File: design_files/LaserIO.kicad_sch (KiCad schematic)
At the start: 25 parts, among them J10 DA15_Receptacle, J11 DB25_Receptacle, U4 74HC245, U5 UA9638CD, U6 UA9638CD, U7 74LVC1G3208

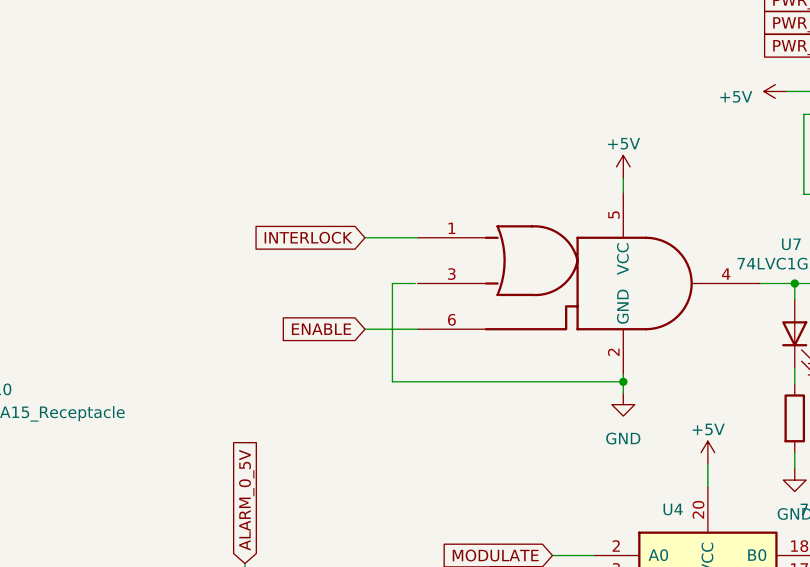
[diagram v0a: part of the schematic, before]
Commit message: And that's why we write documentation - two small errors on the pcb
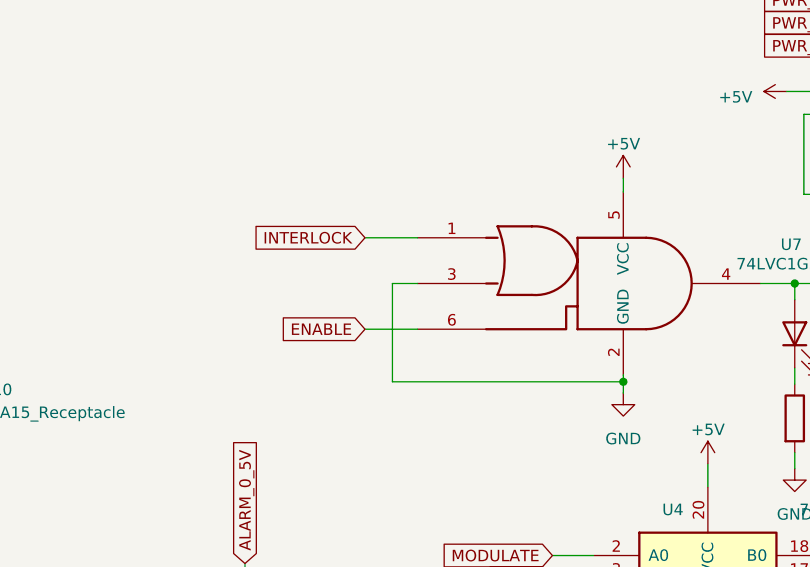
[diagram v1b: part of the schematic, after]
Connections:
- net GND: now also U7.3
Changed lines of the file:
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@@
-    (stroke (width 0) (type default))
-  )
-  (wire (pts (xy 150.368 72.898) (xy 147.828 72.898))
     (stroke (width 0) (type default))
   )
@@
     (stroke (width 0) (type default))
   )
+  (wire (pts (xy 147.828 72.898) (xy 150.622 72.898))
+    (stroke (width 0) (type default))
+  )

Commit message: BOM, readme update
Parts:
- C10, C7, C8, C9: value 0.1uF, 16V -> 0.1uF, 25V; MouserPN (none) -> 187-CL05A104KA5NNNC; mpn (none) -> CL05A104KA5NNNC
- D17: mpn (none) -> 150060GS75000
- D17: mpn (none) -> 150060BS75000
- J10: MouserPN (none) -> 710-618015231321; mpn (none) -> 618015231321
- J11: MouserPN (none) -> 710-618025231121; mpn (none) -> 618025231121
- JP10: value Jumper_2_Open -> Jumper 2 Position, Open
- JP11, JP13, JP9: value e -> Jumper 2 Position, Closed
- U4: MouserPN (none) -> 771-74AHC245PW-Q100J; mpn (none) -> 74AHC245PW-Q100J
- U5, U6: value UA9638CD -> UA9638CDR; MouserPN 296-27141-5-ND -> 595-UA9638CDR
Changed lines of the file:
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@@
       (effects (font (size 1.27 1.27)) hide)
     )
-    (property "Datasheet" "http://www.ti.com/lit/gpn/sn74HC245" (at 210.058 41.402 0)
+    (property "Datasheet" " https://assets.nexperia.com/documents/data-sheet/74AHC_AHCT245_Q100.pdf" (at 210.058 41.402 0)
+      (effects (font (size 1.27 1.27)) hide)
+    )
+    (property "MouserPN" "771-74AHC245PW-Q100J" (at 210.058 41.402 0)
+      (effects (font (size 1.27 1.27)) hide)
+    )
+    (property "mpn" "74AHC245PW-Q100J" (at 210.058 41.402 0)
       (effects (font (size 1.27 1.27)) hide)
     )
@@
       (effects (font (size 1.27 1.27)) (justify left))
     )
-    (property "Value" "UA9638CD" (at 54.2291 96.774 0)
+    (property "Value" "UA9638CDR" (at 54.2291 96.774 0)
       (effects (font (size 1.27 1.27)) (justify left))
     )
@@
       (effects (font (size 1.27 1.27)) hide)
     )
-    (property "MouserPN" "296-27141-5-ND" (at 55.118 105.664 0)
+    (property "MouserPN" "595-UA9638CDR" (at 55.118 105.664 0)
       (effects (font (size 1.27 1.27)) hide)
     )
@@
       (effects (font (size 1.27 1.27)) (justify left))
     )
-    (property "Value" "UA9638CD" (at 54.7371 125.857 0)
+    (property "Value" "UA9638CDR" (at 54.7371 125.857 0)
       (effects (font (size 1.27 1.27)) (justify left))
     )
@@
       (effects (font (size 1.27 1.27)) hide)
     )
-    (property "MouserPN" "296-27141-5-ND" (at 55.626 135.382 0)
+    (property "MouserPN" "595-UA9638CDR" (at 55.626 135.382 0)
       (effects (font (size 1.27 1.27)) hide)
     )
@@
       (effects (font (size 1.27 1.27)))
     )
-    (property "Value" "e" (at 129.667 110.109 0)
+    (property "Value" "Jumper 2 Position, Closed" (at 129.667 110.109 0)
       (effects (font (size 1.27 1.27)) hide)
     )
@@
       (effects (font (size 1.27 1.27)))
     )
-    (property "Value" "0.1uF, 16V" (at 219.456 16.51 90)
+    (property "Value" "0.1uF, 25V" (at 219.456 16.51 90)
       (effects (font (size 1.27 1.27)))
     )
@@
     )
     (property "Datasheet" "~" (at 219.456 20.574 0)
+      (effects (font (size 1.27 1.27)) hide)
+    )
+    (property "MouserPN" "187-CL05A104KA5NNNC" (at 219.456 20.574 0)
+      (effects (font (size 1.27 1.27)) hide)
+    )
+    (property "mpn" "CL05A104KA5NNNC" (at 219.456 20.574 0)
       (effects (font (size 1.27 1.27)) hide)
     )
@@
       (effects (font (size 1.27 1.27)))
     )
-    (property "Value" "e" (at 230.124 126.492 0)
+    (property "Value" "Jumper 2 Position, Closed" (at 230.124 126.492 0)
       (effects (font (size 1.27 1.27)) hide)
     )
@@
       (effects (font (size 1.27 1.27)) hide)
     )
-    (property "Datasheet" "http://www.ti.com/lit/gpn/sn74HC245" (at 182.88 115.824 0)
+    (property "Datasheet" " https://assets.nexperia.com/documents/data-sheet/74AHC_AHCT245_Q100.pdf" (at 182.88 115.824 0)
+      (effects (font (size 1.27 1.27)) hide)
+    )
+    (property "MouserPN" "771-74AHC245PW-Q100J" (at 182.88 115.824 0)
+      (effects (font (size 1.27 1.27)) hide)
+    )
+    (property "mpn" "74AHC245PW-Q100J" (at 182.88 115.824 0)
       (effects (font (size 1.27 1.27)) hide)
     )
@@
       (effects (font (size 1.27 1.27)) (justify left))
     )
-    (property "Value" "UA9638CD" (at 54.9911 61.595 0)
+    (property "Value" "UA9638CDR" (at 54.9911 61.595 0)
       (effects (font (size 1.27 1.27)) (justify left))
     )
@@
       (effects (font (size 1.27 1.27)) hide)
     )
-    (property "MouserPN" "296-27141-5-ND" (at 55.88 71.12 0)
+    (property "MouserPN" "595-UA9638CDR" (at 55.88 71.12 0)
       (effects (font (size 1.27 1.27)) hide)
     )
@@
       (effects (font (size 1.27 1.27)) (justify left))
     )
-    (property "Value" "UA9638CD" (at 54.9911 30.607 0)
+    (property "Value" "UA9638CDR" (at 54.9911 30.607 0)
       (effects (font (size 1.27 1.27)) (justify left))
     )
@@
       (effects (font (size 1.27 1.27)) hide)
     )
-    (property "MouserPN" "296-27141-5-ND" (at 55.88 40.132 0)
+    (property "MouserPN" "595-UA9638CDR" (at 55.88 40.132 0)
       (effects (font (size 1.27 1.27)) hide)
     )
@@
       (effects (font (size 1.27 1.27)) hide)
     )
+    (property "mpn" "150060GS75000" (at 192.532 78.486 0)
+      (effects (font (size 1.27 1.27)) hide)
+    )
     (pin "1")
     (pin "2")
@@
       (effects (font (size 1.27 1.27)))
     )
-    (property "Value" "0.1uF, 16V" (at 59.69 22.86 90)
+    (property "Value" "0.1uF, 25V" (at 59.69 22.86 90)
       (effects (font (size 1.27 1.27)))
     )
@@
       (effects (font (size 1.27 1.27)) hide)
     )
+    (property "MouserPN" "187-CL05A104KA5NNNC" (at 59.69 26.035 0)
+      (effects (font (size 1.27 1.27)) hide)
+    )
+    (property "mpn" "CL05A104KA5NNNC" (at 59.69 26.035 0)
+      (effects (font (size 1.27 1.27)) hide)
+    )
     (pin "1")
     (pin "2")
@@
       (effects (font (size 1.27 1.27)) hide)
     )
-    (property "Datasheet" " ~" (at 98.298 85.344 0)
+    (property "Datasheet" "https://www.we-online.com/katalog/datasheet/6180xx231321.pdf" (at 98.298 85.344 0)
+      (effects (font (size 1.27 1.27)) hide)
+    )
+    (property "MouserPN" "710-618015231321" (at 98.298 85.344 0)
+      (effects (font (size 1.27 1.27)) hide)
+    )
+    (property "mpn" "618015231321" (at 98.298 85.344 0)
       (effects (font (size 1.27 1.27)) hide)
     )
@@
       (effects (font (size 1.27 1.27)))
     )
-    (property "Value" "Jumper_2_Open" (at 244.856 118.11 0)
+    (property "Value" "Jumper 2 Position, Open" (at 244.856 118.11 0)
       (effects (font (size 1.27 1.27)) hide)
     )
@@
       (effects (font (size 1.27 1.27)))
     )
-    (property "Value" "0.1uF, 16V" (at 58.166 90.043 90)
+    (property "Value" "0.1uF, 25V" (at 58.166 90.043 90)
       (effects (font (size 1.27 1.27)))
     )
@@
     )
     (property "Datasheet" "~" (at 58.166 93.218 0)
+      (effects (font (size 1.27 1.27)) hide)
+    )
+    (property "MouserPN" "187-CL05A104KA5NNNC" (at 58.166 93.218 0)
+      (effects (font (size 1.27 1.27)) hide)
+    )
+    (property "mpn" "CL05A104KA5NNNC" (at 58.166 93.218 0)
       (effects (font (size 1.27 1.27)) hide)
     )
@@
       (effects (font (size 1.27 1.27)))
     )
-    (property "Value" "e" (at 244.094 96.012 0)
+    (property "Value" "Jumper 2 Position, Closed" (at 244.094 96.012 0)
       (effects (font (size 1.27 1.27)) hide)
     )
@@
       (effects (font (size 1.27 1.27)) hide)
     )
+    (property "mpn" "150060BS75000" (at 201.803 136.017 0)
+      (effects (font (size 1.27 1.27)) hide)
+    )
     (pin "1")
     (pin "2")
@@
       (effects (font (size 1.27 1.27)) (justify right))
     )
-    (property "Value" "0.1uF, 16V" (at 37.719 176.657 0)
+    (property "Value" "0.1uF, 25V" (at 37.719 176.657 0)
       (effects (font (size 1.27 1.27)) (justify right))
     )
@@
     )
     (property "Datasheet" "~" (at 33.909 174.752 0)
+      (effects (font (size 1.27 1.27)) hide)
+    )
+    (property "MouserPN" "187-CL05A104KA5NNNC" (at 33.909 174.752 0)
+      (effects (font (size 1.27 1.27)) hide)
+    )
+    (property "mpn" "CL05A104KA5NNNC" (at 33.909 174.752 0)
       (effects (font (size 1.27 1.27)) hide)
     )
@@
       (effects (font (size 1.27 1.27)) hide)
     )
+    (property "MouserPN" "710-618025231121" (at 259.08 110.49 0)
+      (effects (font (size 1.27 1.27)) hide)
+    )
+    (property "mpn" "618025231121" (at 259.08 110.49 0)
+      (effects (font (size 1.27 1.27)) hide)
+    )

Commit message: Rev 5a
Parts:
- added R30, R31, R32, R33: R10K, LaserBoardR5:R_0603_1608Metric, symbol Device:R
- C10, C7, C8, C9: Notes (none) -> Generic decoupling cap
- R22, R23, R26, R28, R29: MouserPN (none) -> 603-RC0603JR-0720KL; mpn (none) -> RC0603JR-0720KL
- R24, R25, R27: MouserPN (none) -> 603-RC0603JR-0710KL; mpn (none) -> RC0603JR-0710KL
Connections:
- net ENABLE: now also R30.1
- net GND: now also R30.2, R31.1, R32.1, R33.1
- net GUIDE_LASER: now also R31.2
- net MODULATE: now also R33.2
- net SYNC: now also R32.2
